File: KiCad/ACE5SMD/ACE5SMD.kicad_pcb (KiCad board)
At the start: 2 copper layers, 160 x 100 mm, 90 parts, among them IC1 LM7805_TO220, IC10 74LS273, IC4 74LS04, IC5 74LS02, IC7 74LS365, IC8 74LS30, IC9 74LS365, Q1 2N3904, Q2 5MHz, Q3 BC237, U1 74LS138, X2 CRYSTALHC49U-V 6.556MHz

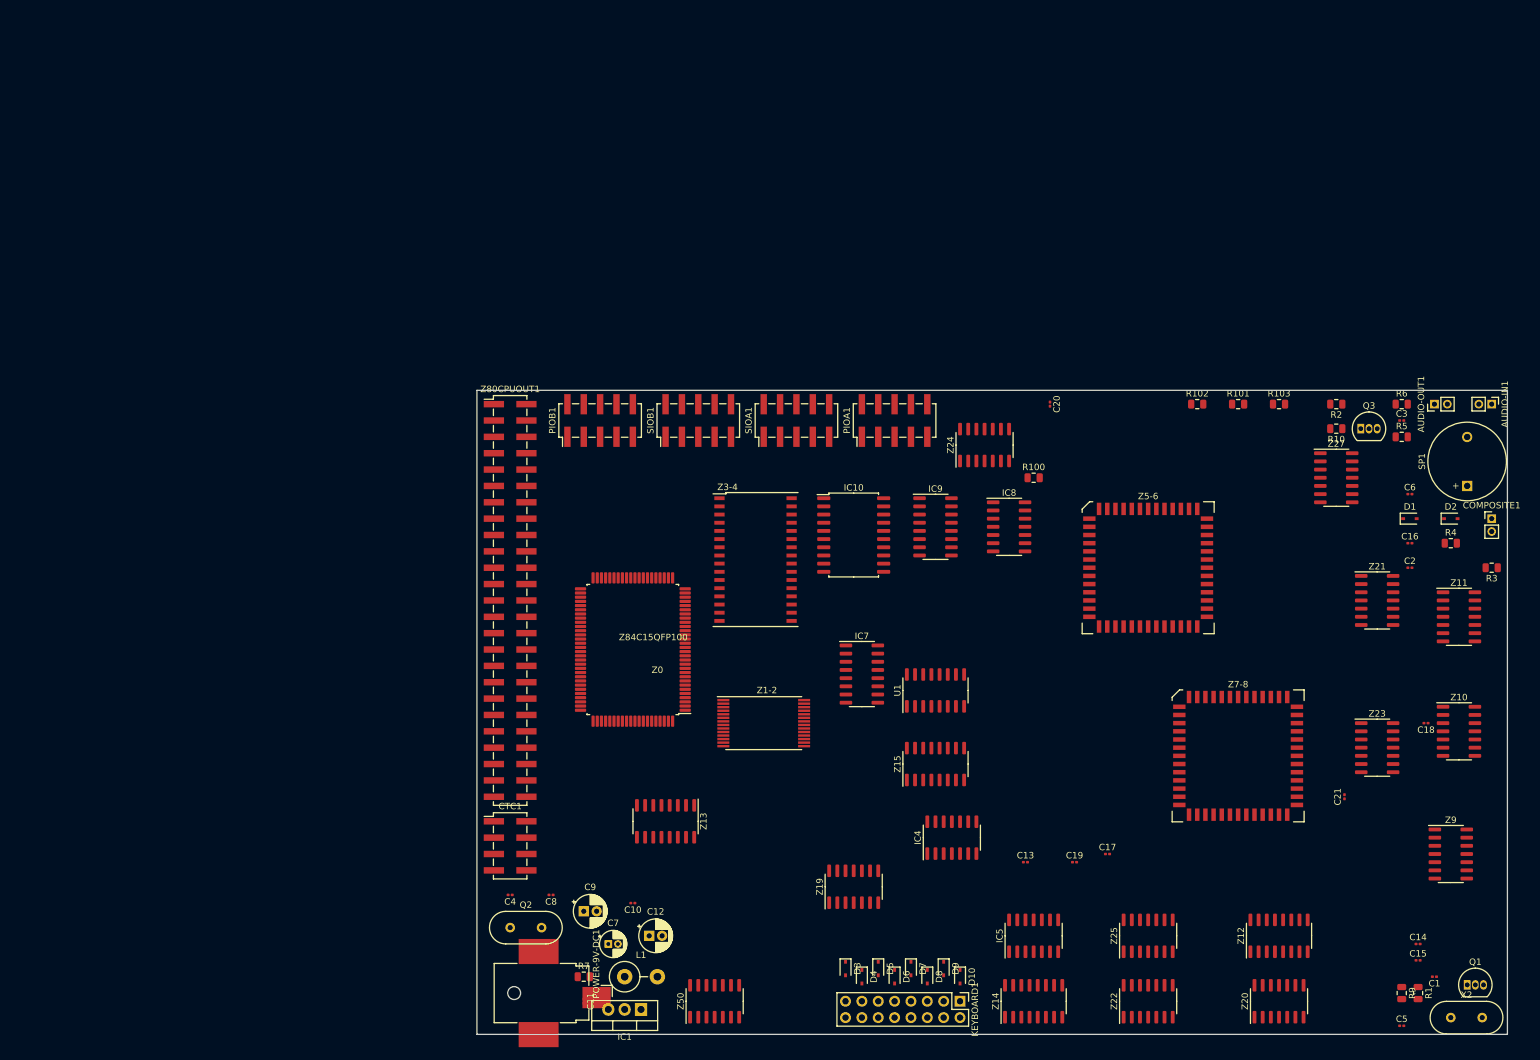
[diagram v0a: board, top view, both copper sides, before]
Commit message: Update numbering. Change footprints.
Signed-off-by: John Bradley <flypie@rocketmail.com>
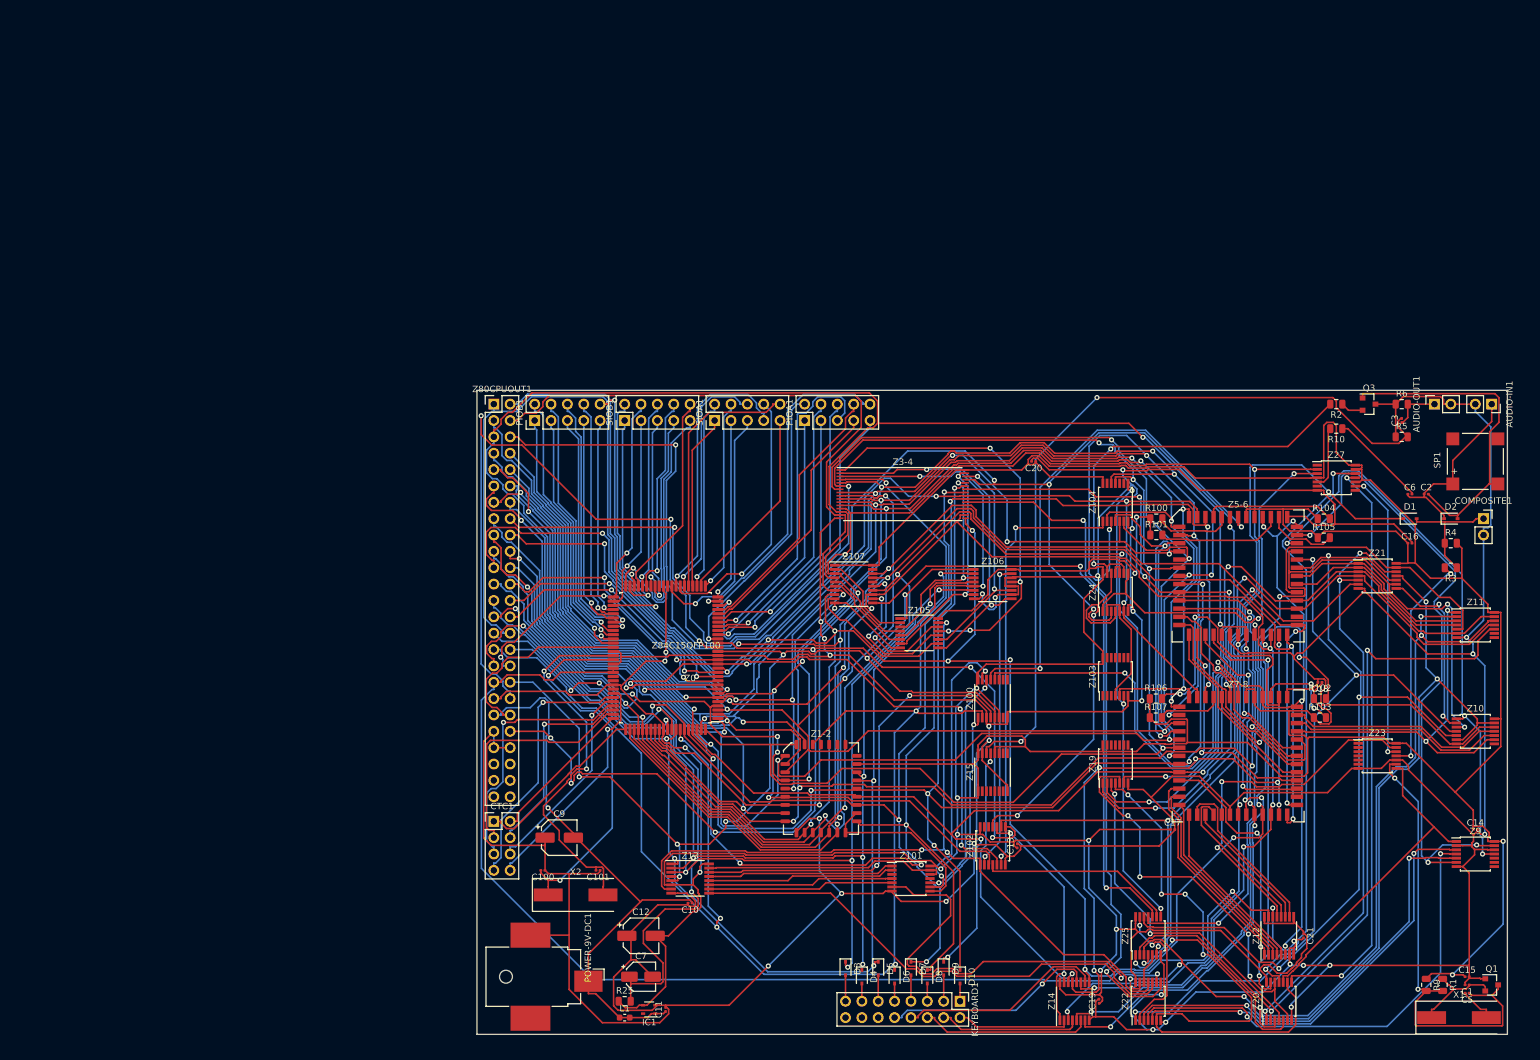
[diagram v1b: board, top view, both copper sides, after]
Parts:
- removed IC5: 74LS02, Package_SO:SOIC-14_3.9x8.7mm_P1.27mm
- removed Z50: 74LS21, Package_SO:SOIC-14_3.9x8.7mm_P1.27mm
- added R104: 270, Resistor_SMD:R_0805_2012Metric, F.Cu at (200.0, 74.9)
- added R105: 270, Resistor_SMD:R_0805_2012Metric, F.Cu at (200.0, 77.9)
- added R106: 270, Resistor_SMD:R_0805_2012Metric, F.Cu at (173.9, 102.9)
- added R107: 270, Resistor_SMD:R_0805_2012Metric, F.Cu at (173.9, 105.8)
- added Z101: 74HCT21, Package_SO:TSSOP-14_4.4x5mm_P0.65mm, F.Cu at (135.9, 130.8)
- added Z103: 74HCT02, Package_SO:TSSOP-14_4.4x5mm_P0.65mm, F.Cu at (167.6, 99.5)
- AUDIO-IN1, AUDIO-OUT1, COMPOSITE1: footprint Connector_PinHeader_2.00mm:PinHeader_1x02_P2.00mm_Vertical -> Connector_PinSocket_2.54mm:PinSocket_1x02_P2.54mm_Vertical
- C100: renamed from C4; value 22p -> 22pf
- C101: renamed from C8; value 42p -> 42pf
- C12: footprint Capacitor_THT:CP_Radial_D5.0mm_P2.00mm -> Capacitor_SMD:CP_Elec_5x3
- C7: value 1U -> 1uf; footprint Capacitor_THT:CP_Radial_D4.0mm_P1.50mm -> Capacitor_SMD:CP_Elec_4x3.9
- C9: value 100u -> 100uf; footprint Capacitor_THT:CP_Radial_D5.0mm_P2.00mm -> Capacitor_SMD:CP_Elec_5x3
- CTC1: footprint Connector_PinHeader_2.54mm:PinHeader_2x04_P2.54mm_Vertical_SMD -> Connector_PinHeader_2.54mm:PinHeader_2x04_P2.54mm_Vertical
- IC1: footprint Package_TO_SOT_THT:TO-220-3_Vertical -> Package_TO_SOT_SMD:SOT-343_SC-70-4
- L1: footprint Inductor_THT:L_Axial_L13.0mm_D4.5mm_P5.08mm_Vertical_Fastron_HCCC -> Inductor_SMD:L_0603_1608Metric
- PIOA1, PIOB1, SIOA1, SIOB1: footprint Connector_PinHeader_2.54mm:PinHeader_2x05_P2.54mm_Vertical_SMD -> Connector_PinHeader_2.54mm:PinHeader_2x05_P2.54mm_Vertical
- Q1: value 2N3904 -> MMBT3904; footprint Package_TO_SOT_THT:TO-92_Inline -> Package_TO_SOT_SMD:SOT-23
- Q3: value BC237 -> BC847; footprint Package_TO_SOT_THT:TO-92_Inline -> Package_TO_SOT_SMD:SOT-23
- R100, R101, R102, R103: value R -> 270
- SP1: footprint Buzzer_Beeper:MagneticBuzzer_ProSignal_ABI-009-RC -> Buzzer_Beeper:PUIAudio_SMT_0825_S_4_R
- X1: renamed from X2; footprint Crystal:Crystal_HC49-U_Vertical -> Crystal:Crystal_SMD_HC49-SD
- X2: renamed from Q2; footprint Crystal:Crystal_HC49-U_Vertical -> Crystal:Crystal_SMD_HC49-SD
- Z1-2: footprint Package_SO:TSOP-I-28_11.8x8mm_P0.55mm -> Package_LCC:PLCC-32_SMD_Socket_11.4x14.0mm_P1.27mm
- Z10, Z11, Z9: value 74LS393 -> 74HCT393; footprint Package_SO:SOIC-14_3.9x8.7mm_P1.27mm -> Package_SO:TSSOP-14_4.4x5mm_P0.65mm
- Z100: renamed from U1; value 74LS138 -> 74HCT138; footprint Package_SO:SOIC-16_3.9x9.9mm_P1.27mm -> Package_SO:TSSOP-16_4.4x5mm_P0.65mm
- Z102: renamed from IC4; value 74LS04 -> 74HCT04; footprint Package_SO:SOIC-14_3.9x8.7mm_P1.27mm -> Package_SO:TSSOP-14_4.4x5mm_P0.65mm
- Z104: renamed from IC8; value 74LS30 -> 74HCT30; footprint Package_SO:SOIC-14_3.9x8.7mm_P1.27mm -> Package_SO:TSSOP-14_4.4x5mm_P0.65mm
- Z105: renamed from IC7; value 74LS365 -> 74HCT365; footprint Package_SO:SOIC-16_3.9x9.9mm_P1.27mm -> Package_SO:TSSOP-16_4.4x5mm_P0.65mm
- Z106: renamed from IC9; value 74LS365 -> 74HCT365; footprint Package_SO:SOIC-16_3.9x9.9mm_P1.27mm -> Package_SO:TSSOP-16_4.4x5mm_P0.65mm
- Z107: renamed from IC10; value 74LS273 -> 74HCT273; footprint Package_SO:SOIC-20W_7.5x12.8mm_P1.27mm -> Package_SO:TSSOP-20_4.4x6.5mm_P0.65mm
- Z12: value 74LS166 -> 74HCT166; footprint Package_SO:SOIC-16_3.9x9.9mm_P1.27mm -> Package_SO:TSSOP-16_4.4x5mm_P0.65mm
- Z13: value 74LS138 -> 74HCT138; footprint Package_SO:SOIC-16_3.9x9.9mm_P1.27mm -> Package_SO:TSSOP-16_4.4x5mm_P0.65mm
- Z14, Z15: value 74LS367 -> 74HCT367; footprint Package_SO:SOIC-16_3.9x9.9mm_P1.27mm -> Package_SO:TSSOP-16_4.4x5mm_P0.65mm
- Z19: value 74LS00 -> 74HCT00; footprint Package_SO:SOIC-14_3.9x8.7mm_P1.27mm -> Package_SO:TSSOP-14_4.4x5mm_P0.65mm
- Z20: value 74LS08 -> 74HCT08; footprint Package_SO:SOIC-14_3.9x8.7mm_P1.27mm -> Package_SO:TSSOP-14_4.4x5mm_P0.65mm
- Z21, Z22: value 74LS11 -> 74HCT11; footprint Package_SO:SOIC-14_3.9x8.7mm_P1.27mm -> Package_SO:TSSOP-14_4.4x5mm_P0.65mm
- Z23: value 74LS86 -> 74HCT86; footprint Package_SO:SOIC-14_3.9x8.7mm_P1.27mm -> Package_SO:TSSOP-14_4.4x5mm_P0.65mm
- Z24, Z25: value 74LS02 -> 74HCT02; footprint Package_SO:SOIC-14_3.9x8.7mm_P1.27mm -> Package_SO:TSSOP-14_4.4x5mm_P0.65mm
- Z27: value 74LS74 -> 74HCT74; footprint Package_SO:SOIC-14_3.9x8.7mm_P1.27mm -> Package_SO:TSSOP-14_4.4x5mm_P0.65mm
- Z3-4: footprint Package_SO:TSOP-II-32_21.0x10.2mm_P1.27mm -> Package_SO:TSOP-I-32_18.4x8mm_P0.5mm
- Z80CPUOUT1: footprint Connector_PinHeader_2.54mm:PinHeader_2x25_P2.54mm_Vertical_SMD -> Connector_PinHeader_2.54mm:PinHeader_2x25_P2.54mm_Vertical
- moved R102 49.5 mm to (199.4, 102.9)
- moved R103 49.1 mm to (199.4, 105.8)
- moved Z19 44.9 mm to (167.6, 113.0)
- moved Z24 30.6 mm to (167.6, 86.4)
- moved Z80CPUOUT1 30.6 mm to (71.1, 57.1)
- moved Z3-4 25.0 mm to (134.6, 71.1)
- moved R101 24.0 mm to (174.0, 77.5)
- moved C21 22.5 mm to (196.8, 139.7), turned to 270 degrees
- moved C19 21.9 mm to (165.1, 149.9), turned to 90 degrees
- moved R100 20.1 mm to (174.0, 74.9)
- moved C14 19.9 mm to (223.5, 123.2)
- moved C18 17.7 mm to (199.4, 100.3)
- moved Z104 16.9 mm to (167.6, 72.4), turned to 90 degrees
- moved Z5-6 14.0 mm to (186.7, 83.8)
- moved PIOA1 14.0 mm to (119.4, 59.7)
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- renumbered R7 to R25
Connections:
- D2 pad 1: Net-(D2-Pad1) -> Net-(AUDIO-IN1-Pad1)
- SP1 pad 1: Net-(D2-Pad1) -> Net-(AUDIO-IN1-Pad1)
- Z102 pad 4: Net-(IC4-Pad4) -> Net-(Z102-Pad4)
- Z104 pad 14: (no net) -> +5V
- Z104 pad 7: (no net) -> GND
- Z104 pad 8: Net-(IC5-Pad2) -> Net-(Z103-Pad6)
- Z25 pad 10: (no net) -> /IOREQ&11111111B
- Z25 pad 8: (no net) -> Net-(Z103-Pad6)
- Z25 pad 9: (no net) -> Net-(Z102-Pad4)
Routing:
- net GND: track 0.00 -> 998.2 mm, vias 0 -> 30
- net +5V: track 0.00 -> 887.7 mm, vias 0 -> 15
- net /DA1: track 0.00 -> 375.9 mm, vias 0 -> 7
- net /DA0: track 0.00 -> 362.6 mm, vias 0 -> 8
- net /DA3: track 0.00 -> 333.6 mm, vias 0 -> 11
- net /DA2: track 0.00 -> 323.3 mm, vias 0 -> 8
- net /DA5: track 0.00 -> 311.4 mm, vias 0 -> 10
- net /A6: track 0.00 -> 283.4 mm, vias 0 -> 6
- net //WR: track 0.00 -> 283.2 mm, vias 0 -> 6
- net /DA6: track 0.00 -> 283.1 mm, vias 0 -> 6
- net /DA7: track 0.00 -> 281.6 mm, vias 0 -> 6
- net /A5: track 0.00 -> 278.0 mm, vias 0 -> 5
- net /DA4: track 0.00 -> 277.3 mm, vias 0 -> 7
- net /A10: track 0.00 -> 276.6 mm, vias 0 -> 7
- net /A8: track 0.00 -> 272.2 mm, vias 0 -> 8
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
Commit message: UPdate to latest version.
Signed-off-by: John Bradley <flypie@rocketmail.com>
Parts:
- added D100: BAT54W, Package_TO_SOT_SMD:SOT-323_SC-70, F.Cu at (154.4, 118.2)
- added HBL1: MountingHole, MountingHole:MountingHole_2.5mm, F.Cu at (82.0, 136.0)
- added HBR1: MountingHole, MountingHole:MountingHole_2.5mm, F.Cu at (212.0, 136.0)
- added HTL1: MountingHole, MountingHole:MountingHole_2.5mm, F.Cu at (82.0, 56.0)
- added HTR1: MountingHole, MountingHole:MountingHole_2.5mm, F.Cu at (212.0, 56.0)
- AUDIO-IN1, AUDIO-OUT1, COMPOSITE1: footprint Connector_PinSocket_2.54mm:PinSocket_1x02_P2.54mm_Vertical -> Connector_PinHeader_2.54mm:PinHeader_1x02_P2.54mm_Vertical
- IC1: footprint Package_TO_SOT_SMD:SOT-343_SC-70-4 -> Package_TO_SOT_SMD:SOT-223-3_TabPin2
- L1: value L -> 100 nH
- POWER-9V-DC1: value Conn_01x02 -> PJ-036C; footprint Connector_BarrelJack:BarrelJack_CUI_PJ-036AH-SMT_Horizontal -> cuipj:CUI_PJ-036C
- R1, R10, R100, R101, R102, R103, R104, R105, R106, R107, R2, R25, R3, R4, R5, R6, R9: footprint Resistor_SMD:R_0805_2012Metric -> Resistor_SMD:R_0603_1608Metric
- Z3-4: footprint Package_SO:TSOP-I-32_18.4x8mm_P0.5mm -> Package_BGA:FBGA-48_6x8_6.0x8.0mm
- moved C15 83.8 mm to (162.3, 87.5)
- moved R25 43.8 mm to (106.4, 108.8)
- moved C20 38.0 mm to (117.0, 65.0)
- moved C18 37.3 mm to (194.1, 63.4)
- moved C7 35.7 mm to (106.4, 112.6)
- moved Z106 32.0 mm to (130.0, 59.0), turned to 90 degrees
- moved C10 23.5 mm to (80.0, 144.0), turned to 270 degrees
- moved Z107 20.7 mm to (114.0, 69.0)
- moved C9 17.9 mm to (85.0, 142.0), turned to 90 degrees
- moved IC1 17.6 mm to (91.0, 134.0)
- moved C6 15.5 mm to (215.7, 55.8)
- moved D10 15.4 mm to (131.0, 137.0)
- moved D4 15.4 mm to (115.8, 137.0)
- moved D8 15.4 mm to (125.9, 137.0)
- moved KEYBOARD1 15.4 mm to (131.0, 140.9)
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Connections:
- POWER-9V-DC1 pad 3: (no net) -> Net-(POWER-9V-DC1-Pad3)
- Z102 pad 8: //INT -> Net-(D100-Pad3)
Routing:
- net /A6: track 283.4 -> 196.1 mm
- net /A12: track 247.3 -> 163.0 mm
- net /A5: track 278.0 -> 204.3 mm, vias 5 -> 6
- net //HALT: track 108.3 -> 37.7 mm, vias 3 -> 2
- net /A2: track 271.3 -> 202.9 mm, vias 10 -> 6
- net /DA6: track 283.1 -> 349.8 mm, vias 6 -> 4
- net /DA1: track 375.9 -> 310.1 mm, vias 7 -> 9
- net /A7: track 253.2 -> 188.8 mm, vias 9 -> 5
- net #RESET: track 114.6 -> 69.5 mm
- net /A11: track 201.3 -> 244.4 mm, vias 6 -> 5
- net //IOREQ: track 115.6 -> 157.4 mm, vias 5 -> 2
- net +5V: track 887.7 -> 848.7 mm, vias 15 -> 11
- net /A8: track 272.2 -> 237.8 mm
- net //INT: track 159.6 -> 125.6 mm, vias 6 -> 5
- net GND: track 998.2 -> 965.2 mm, vias 30 -> 11
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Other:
- net class Default: trace_width 0.25 -> 0.2
- net class SMD added: clearance 0.1524, trace_width 0.2, via_dia 0.8, via_drill 0.4
